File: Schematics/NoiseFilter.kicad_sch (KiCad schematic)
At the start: 167 parts

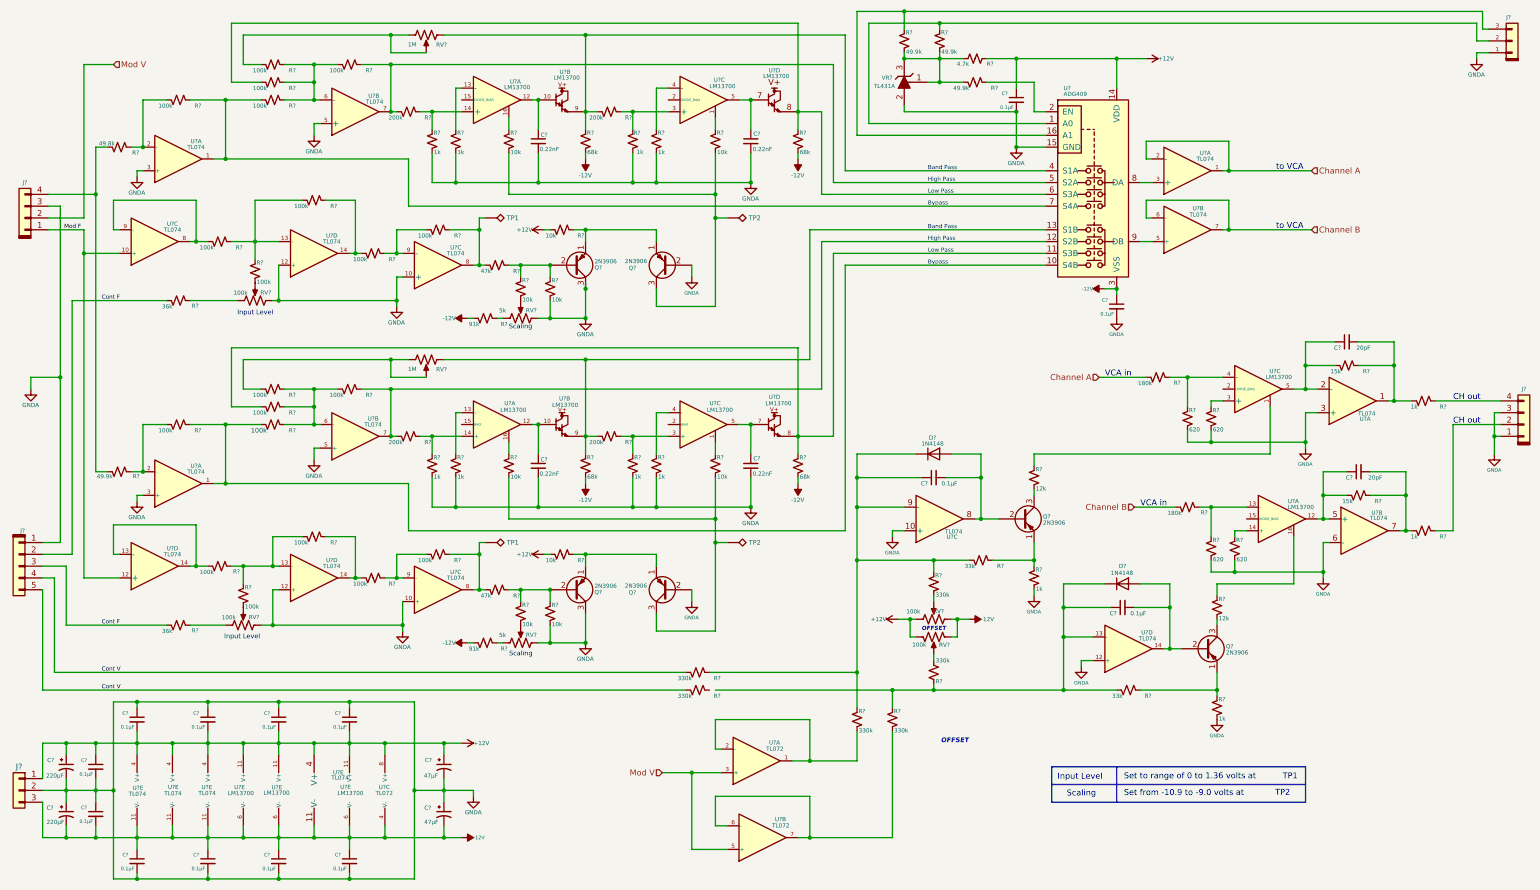
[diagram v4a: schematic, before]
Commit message: - Updated current libraries - New 7 inc display with ESP32S3 and second USB upload port - Start of I2C feeder interface slave on display.
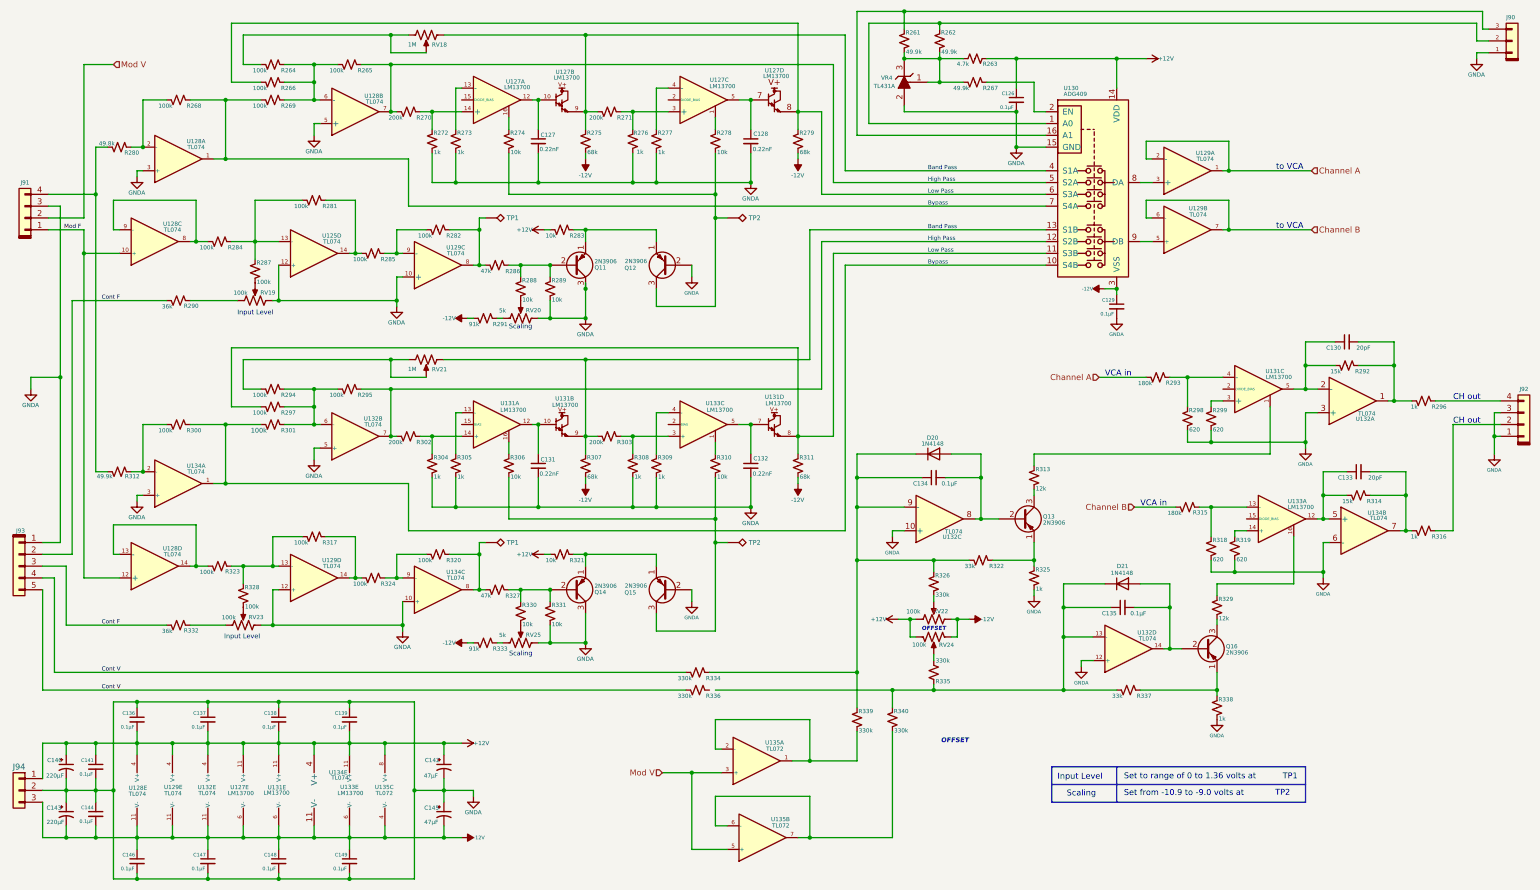
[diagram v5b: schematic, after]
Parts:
- gave numbers to parts that had none: 140
